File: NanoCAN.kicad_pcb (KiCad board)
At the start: 2 copper layers, 43.4 x 18 mm, 18 parts, among them J2 Screw_Terminal_01x02, J3 Screw_Terminal_01x02, SW1 SW_DIP_x01, U1 MCP2557FD-xSN, U3 MCP2517FD-xJHA, Y1 Crystal_GND24

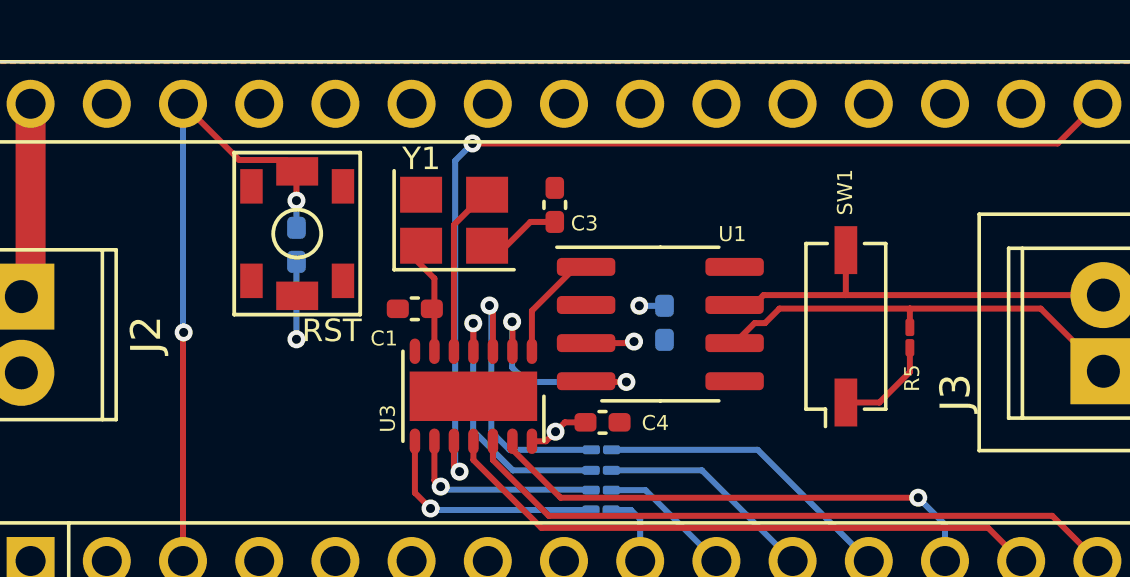
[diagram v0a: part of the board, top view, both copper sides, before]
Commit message: Swap pushbutton for PTS810 and create 3D Model
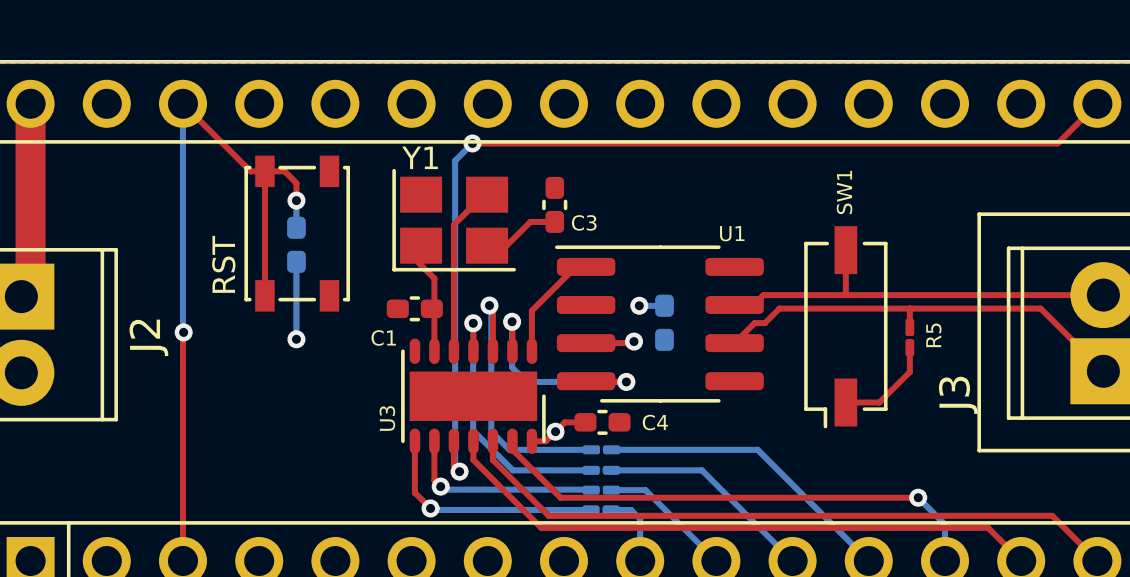
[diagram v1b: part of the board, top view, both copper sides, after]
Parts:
- PB1: value TACTILE1PTS820-NH -> SW_Push; footprint NANOEveryV3.0:C&K_PTS820_NO_HOLES -> Button_Switch_SMD:SW_SPST_PTS810
- turned PB1 to -90 degrees
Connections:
- PB1 pad 2: GND -> /RESETN
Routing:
- net /RESETN: track 21.9 -> 25.8 mm
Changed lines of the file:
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@@
     )
   )
-  (footprint "NANOEveryV3.0:C&K_PTS820_NO_HOLES" (layer "F.Cu")
-    (at 138.8872 124.0868 90)
-    (property "Sheetfile" "NanoCAN.kicad_sch")
-    (property "Sheetname" "")
-    (fp_text reference "PB1" (at -4.6658 -0.1524 180) (layer "F.SilkS") hide
-        (effects (font (size 1 1) (thickness 0.15)))
-    )
-    (fp_text value "TACTILE1PTS820-NH" (at 0 0 90) (layer "F.Fab") hide
-        (effects (font (size 1.27 1.27) (thickness 0.15)))
-    )
-    (fp_line (start -2.7 -2.1) (end -2.7 2.1)
-      (stroke (width 0.127) (type solid)) (layer "F.SilkS"))
-    (fp_line (start -2.7 2.1) (end 2.7 2.1)
-      (stroke (width 0.127) (type solid)) (layer "F.SilkS"))
-    (fp_line (start 2.7 -2.1) (end -2.7 -2.1)
-      (stroke (width 0.127) (type solid)) (layer "F.SilkS"))
-    (fp_line (start 2.7 2.1) (end 2.7 -2.1)
-      (stroke (width 0.127) (type solid)) (layer "F.SilkS"))
-    (fp_circle (center 0 0) (end 0.8 0)
-      (stroke (width 0.127) (type solid)) (fill none) (layer "F.SilkS"))
-    (pad "1" smd rect (at -1.575 -1.525 270) (size 1.15 0.75) (layers "F.Cu" "F.Paste" "F.Mask")
-      (net 1 "GND") (pinfunction "3") (pintype "power_in") (solder_mask_margin 0.1016) (thermal_bridge_angle 45))
-    (pad "2" smd rect (at -1.575 1.525 270) (size 1.15 0.75) (layers "F.Cu" "F.Paste" "F.Mask")
-      (net 1 "GND") (pinfunction "3") (pintype "power_in") (solder_mask_margin 0.1016) (thermal_bridge_angle 45))
-    (pad "3" smd rect (at 1.575 -1.525 270) (size 1.15 0.75) (layers "F.Cu" "F.Paste" "F.Mask")
-      (net 1 "GND") (pinfunction "3") (pintype "power_in") (solder_mask_margin 0.1016) (thermal_bridge_angle 45))
-    (pad "4" smd rect (at 1.575 1.525 270) (size 1.15 0.75) (layers "F.Cu" "F.Paste" "F.Mask")
-      (net 1 "GND") (pinfunction "3") (pintype "power_in") (solder_mask_margin 0.1016) (thermal_bridge_angle 45))
-    (pad "5" smd rect (at -2.075 0 180) (size 1.4 0.95) (layers "F.Cu" "F.Paste" "F.Mask")
-      (net 1 "GND") (pinfunction "1") (pintype "passive") (solder_mask_margin 0.1016) (thermal_bridge_angle 45))
-    (pad "6" smd rect (at 2.075 0 180) (size 1.4 0.95) (layers "F.Cu" "F.Paste" "F.Mask")
-      (net 2 "/RESETN") (pinfunction "2") (pintype "passive") (solder_mask_margin 0.1016) (thermal_bridge_angle 45))
-    (model "C:/Users/avander/Downloads/LIB_PTS820J20KPSMTRLFS/PTS820J20KPSMTRLFS/3D/PTS820J20KPSMTRLFS.stp"
-      (offset (xyz 0 0 0))
-      (scale (xyz 1 1 1))
-      (rotate (xyz 0 0 0))
+  (footprint "Button_Switch_SMD:SW_SPST_PTS810" (layer "F.Cu")
+    (at 138.8872 124.0868 -90)
+    (descr "C&K Components, PTS 810 Series, Microminiature SMT Top Actuated, http://www.ckswitches.com/media/1476/pts810.pdf")
+    (tags "SPST Button Switch")
+    (property "Sheetfile" "NanoCAN.kicad_sch")
+    (property "Sheetname" "")
+    (property "ki_description" "Push button switch, generic, two pins")
+    (property "ki_keywords" "switch normally-open pushbutton push-button")
+    (attr smd)
+    (fp_text reference "PB1" (at -0.211 2.54 90) (layer "F.SilkS") hide
+        (effects (font (size 1 1) (thickness 0.15)))
+    )
+    (fp_text value "SW_Push" (at 0 2.6 90) (layer "F.Fab") hide
+        (effects (font (size 1 1) (thickness 0.15)))
+    )
+    (fp_text user "${REFERENCE}" (at 0 0 90) (layer "F.Fab")
+        (effects (font (size 0.6 0.6) (thickness 0.09)))
+    )
+    (fp_line (start -2.2 -1.7) (end -2.2 -1.58)
+      (stroke (width 0.12) (type solid)) (layer "F.SilkS"))
+    (fp_line (start -2.2 -0.57) (end -2.2 0.57)
+      (stroke (width 0.12) (type solid)) (layer "F.SilkS"))
+    (fp_line (start -2.2 1.58) (end -2.2 1.7)
+      (stroke (width 0.12) (type solid)) (layer "F.SilkS"))
+    (fp_line (start -2.2 1.7) (end 2.2 1.7)
+      (stroke (width 0.12) (type solid)) (layer "F.SilkS"))
+    (fp_line (start 2.2 -1.7) (end -2.2 -1.7)
+      (stroke (width 0.12) (type solid)) (layer "F.SilkS"))
+    (fp_line (start 2.2 -1.58) (end 2.2 -1.7)
+      (stroke (width 0.12) (type solid)) (layer "F.SilkS"))
+    (fp_line (start 2.2 0.57) (end 2.2 -0.57)
+      (stroke (width 0.12) (type solid)) (layer "F.SilkS"))
+    (fp_line (start 2.2 1.7) (end 2.2 1.58)
+      (stroke (width 0.12) (type solid)) (layer "F.SilkS"))
+    (fp_line (start -2.85 -1.85) (end 2.85 -1.85)
+      (stroke (width 0.05) (type solid)) (layer "F.CrtYd"))
+    (fp_line (start -2.85 1.85) (end -2.85 -1.85)
+      (stroke (width 0.05) (type solid)) (layer "F.CrtYd"))
+    (fp_line (start 2.85 -1.85) (end 2.85 1.85)
+      (stroke (width 0.05) (type solid)) (layer "F.CrtYd"))
+    (fp_line (start 2.85 1.85) (end -2.85 1.85)
+      (stroke (width 0.05) (type solid)) (layer "F.CrtYd"))
+    (fp_line (start -2.1 -1.6) (end -2.1 1.6)
+      (stroke (width 0.1) (type solid)) (layer "F.Fab"))
+    (fp_line (start -2.1 1.6) (end 2.1 1.6)
+      (stroke (width 0.1) (type solid)) (layer "F.Fab"))
+    (fp_line (start -0.4 -1.1) (end 0.4 -1.1)
+      (stroke (width 0.1) (type solid)) (layer "F.Fab"))
+    (fp_line (start 0.4 1.1) (end -0.4 1.1)
+      (stroke (width 0.1) (type solid)) (layer "F.Fab"))
+    (fp_line (start 2.1 -1.6) (end -2.1 -1.6)
+      (stroke (width 0.1) (type solid)) (layer "F.Fab"))
+    (fp_line (start 2.1 1.6) (end 2.1 -1.6)
+      (stroke (width 0.1) (type solid)) (layer "F.Fab"))
+    (fp_arc (start -0.4 1.1) (mid -1.5 0) (end -0.4 -1.1)
+      (stroke (width 0.1) (type solid)) (layer "F.Fab"))
+    (fp_arc (start 0.4 -1.1) (mid 1.5 0) (end 0.4 1.1)
+      (stroke (width 0.1) (type solid)) (layer "F.Fab"))
+    (pad "1" smd rect (at -2.075 -1.075 270) (size 1.05 0.65) (layers "F.Cu" "F.Paste" "F.Mask")
+      (net 1 "GND") (pinfunction "1") (pintype "passive"))
+    (pad "1" smd rect (at 2.075 -1.075 270) (size 1.05 0.65) (layers "F.Cu" "F.Paste" "F.Mask")
+      (net 1 "GND") (pinfunction "1") (pintype "passive"))
+    (pad "2" smd rect (at -2.075 1.075 270) (size 1.05 0.65) (layers "F.Cu" "F.Paste" "F.Mask")
+      (net 2 "/RESETN") (pinfunction "2") (pintype "passive"))
+    (pad "2" smd rect (at 2.075 1.075 270) (size 1.05 0.65) (layers "F.Cu" "F.Paste" "F.Mask")
+      (net 2 "/RESETN") (pinfunction "2") (pintype "passive"))
+    (model "${KIPRJMOD}/3dmodels/Button_PTS810.step"
+      (offset (xyz 0 0 0))
+      (scale (xyz 1 1 1))
+      (rotate (xyz 0 0 90))
     )
   )
@@
     (property "ki_keywords" "R res resistor")
     (attr smd)
-    (fp_text reference "R5" (at 1.3531 -0.0762 90) (layer "F.SilkS")
+    (fp_text reference "R5" (at -0.0693 -0.8128 90) (layer "F.SilkS")
         (effects (font (size 0.5 0.5) (thickness 0.125)))
     )
@@
   (gr_line (start 169.4942 136.398) (end 126.0602 136.398)
     (stroke (width 0.01) (type solid)) (layer "Edge.Cuts"))
-  (gr_text "RST" (at 139.0396 127.762) (layer "F.SilkS")
+  (gr_text "RST" (at 136.906 126.1618 90) (layer "F.SilkS")
     (effects (font (size 0.75 0.75) (thickness 0.1)) (justify left bottom))
   )
@@
   (segment (start 151.13 126.492) (end 150.2918 126.492) (width 0.2) (layer "B.Cu") (net 1))
   (segment (start 138.8618 125.0275) (end 138.8618 127.6096) (width 0.2) (layer "B.Cu") (net 1))
-  (segment (start 138.509 121.6336) (end 136.9536 121.6336) (width 0.2) (layer "F.Cu") (net 2))
-  (segment (start 138.8618 122.9868) (end 138.8618 122.0372) (width 0.2) (layer "F.Cu") (net 2))
+  (segment (start 137.3318 122.0118) (end 135.08 119.76) (width 0.2) (layer "F.Cu") (net 2))
   (segment (start 135.08 127.4036) (end 135.08 135) (width 0.2) (layer "F.Cu") (net 2))
-  (segment (start 138.8872 122.0118) (end 138.509 121.6336) (width 0.2) (layer "F.Cu") (net 2))
-  (segment (start 138.8618 122.0372) (end 138.8872 122.0118) (width 0.2) (layer "F.Cu") (net 2))
-  (segment (start 136.9536 121.6336) (end 135.08 119.76) (width 0.2) (layer "F.Cu") (net 2))
+  (segment (start 138.8618 122.9868) (end 138.8618 122.4026) (width 0.2) (layer "F.Cu") (net 2))
+  (segment (start 137.8122 122.0118) (end 137.8122 126.1618) (width 0.2) (layer "F.Cu") (net 2))
+  (segment (start 137.8122 122.0118) (end 137.3318 122.0118) (width 0.2) (layer "F.Cu") (net 2))
+  (segment (start 138.8618 122.4026) (end 138.471 122.0118) (width 0.2) (layer "F.Cu") (net 2))
   (segment (start 135.1026 127.381) (end 135.08 127.4036) (width 0.2) (layer "F.Cu") (net 2))
+  (segment (start 138.471 122.0118) (end 137.8122 122.0118) (width 0.2) (layer "F.Cu") (net 2))
   (via (at 135.1026 127.381) (size 0.6) (drill 0.3) (layers "F.Cu" "B.Cu") (net 2))
   (via (at 138.8618 122.9868) (size 0.6) (drill 0.3) (layers "F.Cu" "B.Cu") (net 2))

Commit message: Update to MCP251863 to combine transciever and SPI converter
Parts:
- removed U1: MCP2557FD-xSN, Package_SO:SOIC-8_3.9x4.9mm_P1.27mm
- removed U3: MCP2517FD-xJHA, Package_DFN_QFN:DFN-14-1EP_3x4.5mm_P0.65mm_EP1.65x4.25mm
- added C6: 100n, Capacitor_SMD:C_0402_1005Metric_Pad0.74x0.62mm_HandSolder, F.Cu at (189.3, 117.9)
- added R6: 0R, Resistor_SMD:R_01005_0402Metric_Pad0.57x0.30mm_HandSolder, F.Cu at (189.0, 119.7)
- added U2: MCP2517FD-xSL, Package_SO:SSOP-28_5.3x10.2mm_P0.65mm, F.Cu at (182.5, 122.9)
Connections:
- A1 pad 8: /D5~{} -> D5~{}
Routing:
- net (no net): track 0.00 -> 14.0 mm, vias 0 -> 2
- net Net-(U1-RXD): track 7.88 -> 0.00 mm, vias 2 -> 0
- net Net-(U1-TXD): track 3.76 -> 0.00 mm
- net Net-(U2-OSC2): track 8.09 -> 5.74 mm
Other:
- copper layers 2 -> 4

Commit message: fixup! Update to MCP251863 to combine transciever and SPI converter
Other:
- copper layers 4 -> 2
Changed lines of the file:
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@@
 (kicad_pcb (version 20221018) (generator pcbnew)
   (general
-    (thickness 1.6)
+    (thickness 1.6152)
   )
   (paper "A4")
   (layers
     (0 "F.Cu" signal)
-    (1 "In1.Cu" signal)
-    (2 "In2.Cu" signal)
     (31 "B.Cu" signal)
     (32 "B.Adhes" user "B.Adhesive")

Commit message: Fix netclass for CAN
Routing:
- net /CAN-: track 14.3 -> 0.63 mm
- net /CAN+: track 14.6 -> 1.50 mm
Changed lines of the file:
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@@
         (effects (font (size 1 1) (thickness 0.15)))
-    )
-    (fp_text user "on" (at 0.83 -0.76 90) (layer "F.Fab")
-        (effects (font (size 0.6 0.6) (thickness 0.09)))
     )
     (fp_text user "${REFERENCE}" (at 2.1 0 180) (layer "F.Fab")
@@
   (segment (start 144.1514 131.873014) (end 144.29967 132.021284) (width 0.2) (layer "B.Cu") (net 28))
   (segment (start 159.3088 127.2144) (end 159.3088 126.586401) (width 0.2) (layer "F.Cu") (net 29))
-  (segment (start 154.479522 127.0698) (end 154.962921 126.586401) (width 0.2) (layer "F.Cu") (net 29))
-  (segment (start 159.3088 126.586401) (end 163.670401 126.586401) (width 0.2) (layer "F.Cu") (net 29))
-  (segment (start 154.962921 126.586401) (end 159.3088 126.586401) (width 0.2) (layer "F.Cu") (net 29))
-  (segment (start 163.670401 126.586401) (end 165.7604 128.6764) (width 0.2) (layer "F.Cu") (net 29))
-  (segment (start 154.1336 127.0698) (end 154.479522 127.0698) (width 0.2) (layer "F.Cu") (net 29))
-  (segment (start 153.4668 127.7366) (end 154.1336 127.0698) (width 0.2) (layer "F.Cu") (net 29))
-  (segment (start 153.4668 126.4666) (end 154.100403 126.4666) (width 0.2) (layer "F.Cu") (net 30))
   (segment (start 157.1752 126.1364) (end 157.1752 124.6378) (width 0.2) (layer "F.Cu") (net 30))
-  (segment (start 157.1752 126.1364) (end 165.7604 126.1364) (width 0.2) (layer "F.Cu") (net 30))
-  (segment (start 153.4668 126.4666) (end 154.1526 126.4666) (width 0.2) (layer "F.Cu") (net 30))
-  (segment (start 154.430603 126.1364) (end 157.1752 126.1364) (width 0.2) (layer "F.Cu") (net 30))
-  (segment (start 154.100403 126.4666) (end 154.430603 126.1364) (width 0.2) (layer "F.Cu") (net 30))
   (segment (start 143.46105 125.58385) (end 142.6674 124.7902) (width 0.2) (layer "F.Cu") (net 32))
   (segment (start 143.46105 128.0085) (end 143.46105 125.58385) (width 0.2) (layer "F.Cu") (net 32))
